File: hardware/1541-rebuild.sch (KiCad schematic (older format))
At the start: 8 parts, among them IC1 ATMEGA1284P-P, P1 1541_CN3, P2 1541_CN4_PIN7_[MOTOR], X1 20Mhz

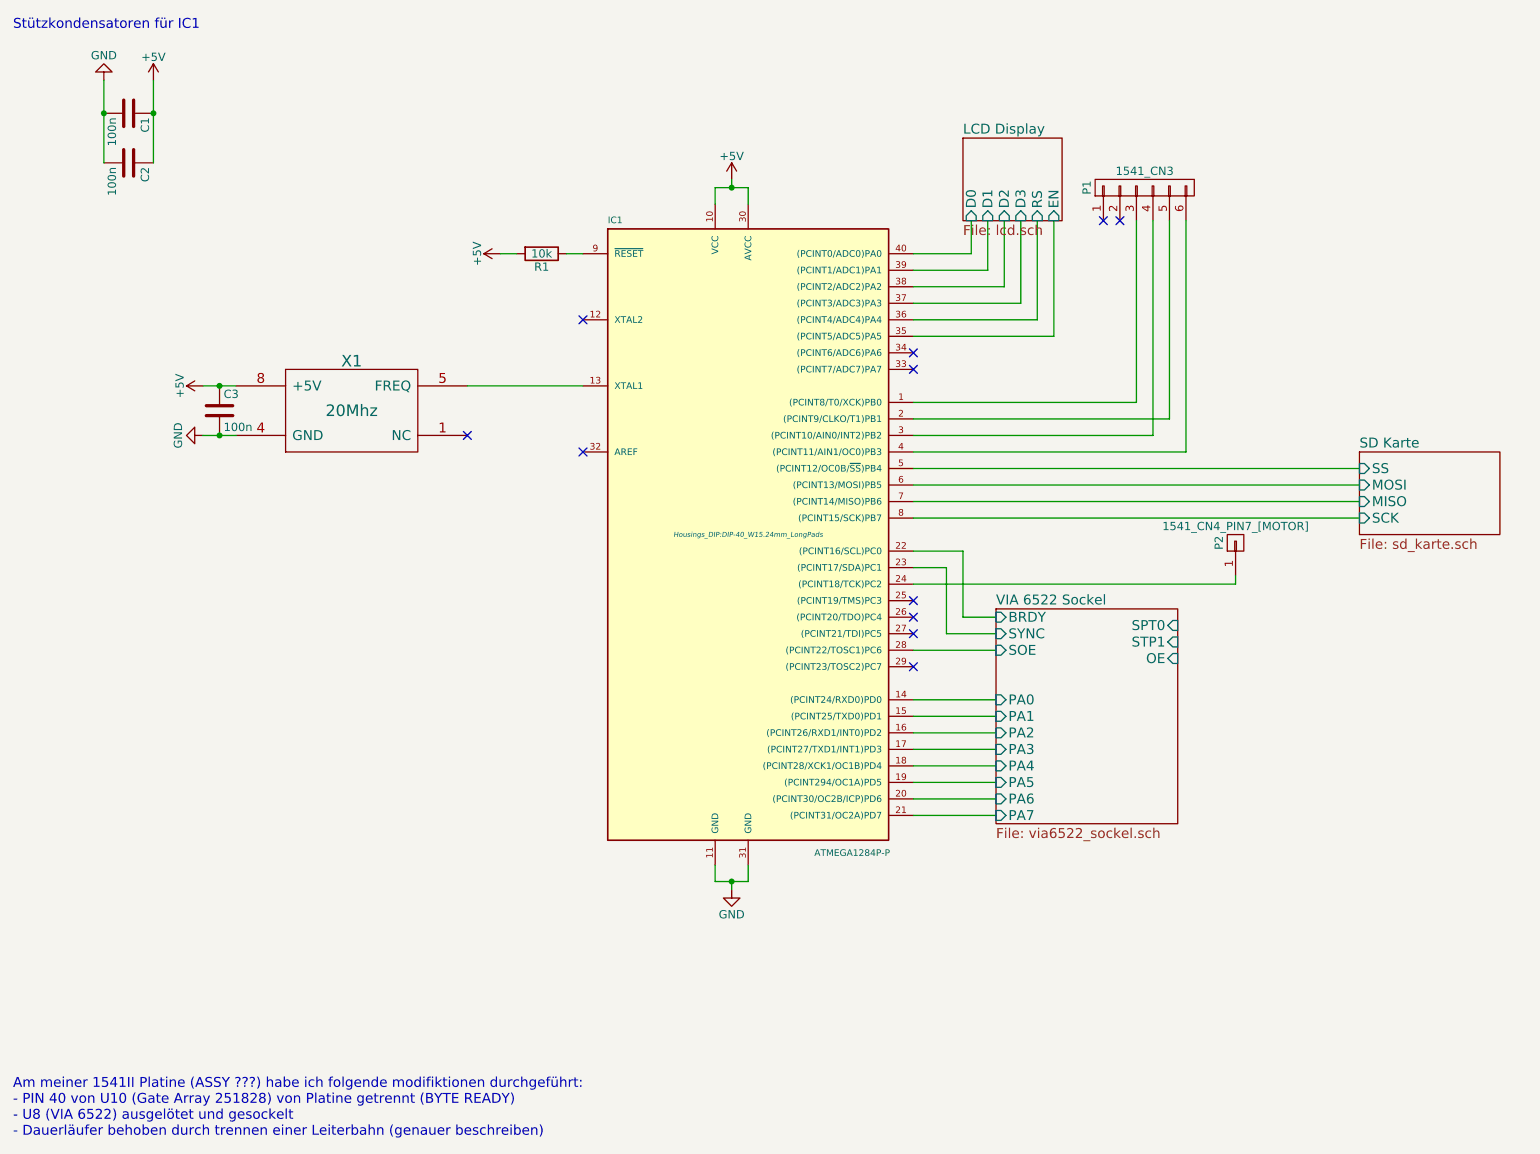
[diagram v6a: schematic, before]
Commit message: Sourcecode neu überarbeitet, Schaltplan angepasst und DOC bearbeitet
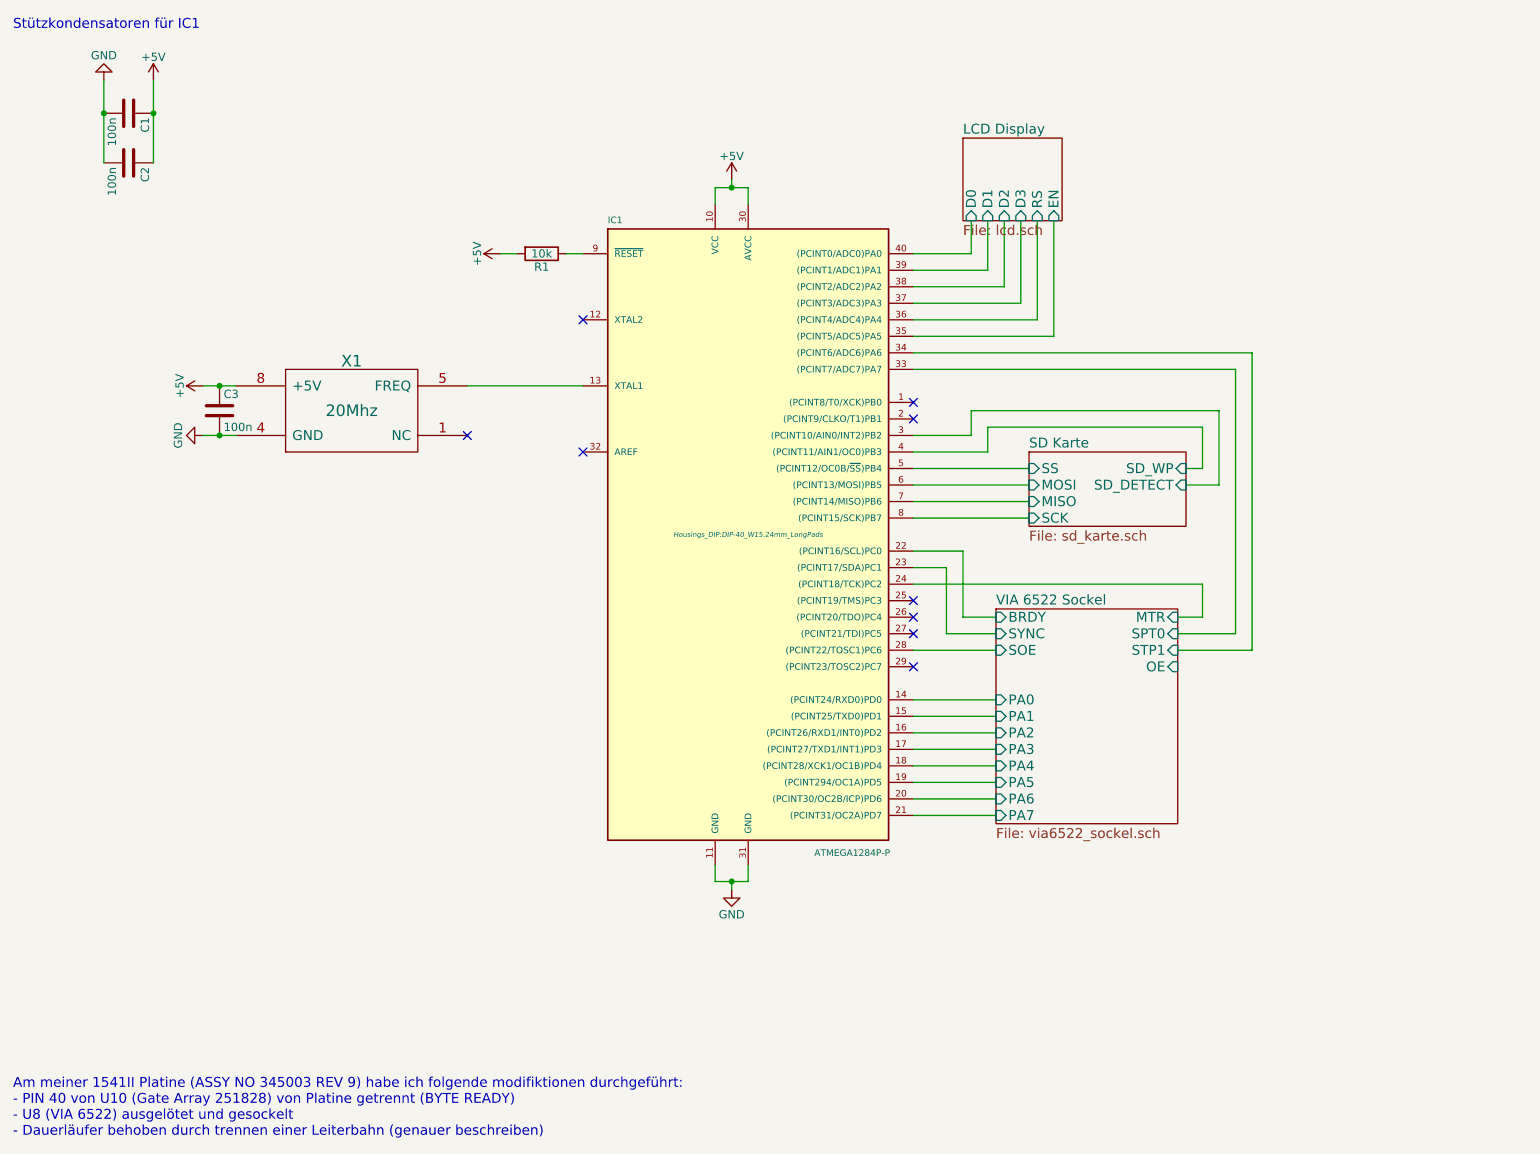
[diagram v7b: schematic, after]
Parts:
- removed P1: 1541_CN3, Socket_Strips:Socket_Strip_Straight_1x06, symbol CONN_01X06
- removed P2: 1541_CN4_PIN7_[MOTOR], Pin_Headers:Pin_Header_Straight_1x01, symbol CONN_01X01
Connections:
- net VIA 6522 Sockel/SPT0: now also IC1.33 ((PCINT7/ADC7)PA7)
- net VIA 6522 Sockel/STP1: now also IC1.34 ((PCINT6/ADC6)PA6)
- net VIA 6522 Sockel/MTR: now reaches IC1.24 ((PCINT18/TCK)PC2)
- net SD Karte/SD_DETECT: now reaches IC1.3 ((PCINT10/AIN0/INT2)PB2)
- net SD Karte/SD_WP: now reaches IC1.4 ((PCINT11/AIN1/OC0)PB3)
- no-connect marks 11 -> 9
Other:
- note added: "Am meiner 1541II Platine (ASSY NO 345003 REV 9) habe ich folgende modifiktionen durchgeführt:\n- PIN 40 von U10 (Gate Array 251828) von Platine getrennt (BYTE READY)\n- U8 (VIA 6522) ausgelötet und gesockelt\n- Dauerläufer behoben durch trennen einer Leiterbahn (genauer beschreiben)"
- note removed: "Am meiner 1541II Platine (ASSY ???) habe ich folgende modifiktionen durchgeführt:\n- PIN 40 von U10 (Gate Array 251828) von Platine getrennt (BYTE READY)\n- U8 (VIA 6522) ausgelötet und gesockelt\n- Dauerläufer behoben durch trennen einer Leiterbahn (genauer beschreiben)"
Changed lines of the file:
@@
 $EndComp
 Text Notes 650  7450 0    60   ~ 0
-Am meiner 1541II Platine (ASSY ???) habe ich folgende modifiktionen durchgeführt:\n- PIN 40 von U10 (Gate Array 251828) von Platine getrennt (BYTE READY)\n- U8 (VIA 6522) ausgelötet und gesockelt\n- Dauerläufer behoben durch trennen einer Leiterbahn (genauer beschreiben)
+Am meiner 1541II Platine (ASSY NO 345003 REV 9) habe ich folgende modifiktionen durchgeführt:\n- PIN 40 von U10 (Gate Array 251828) von Platine getrennt (BYTE READY)\n- U8 (VIA 6522) ausgelötet und gesockelt\n- Dauerläufer behoben durch trennen einer Leiterbahn (genauer beschreiben)
 $Comp
 L TCXO3 X1
@@
 	1    0    0    -1
 $EndComp
-Wire Wire Line
-	3400 2900 4100 2900
 NoConn ~ 3400 3200
 $Comp
@@
 	1    0    0    -1
 $EndComp
-Wire Wire Line
-	1800 2900 2000 2900
-Connection ~ 1900 2900
-Wire Wire Line
-	1800 3200 2000 3200
-Connection ~ 1900 3200
 NoConn ~ 4100 2500
 $Comp
@@
 	1    0    0    -1
 $EndComp
-Wire Wire Line
-	4900 5800 4900 5900
-Wire Wire Line
-	4900 5900 5100 5900
-Wire Wire Line
-	5000 5900 5000 5950
-Wire Wire Line
-	5100 5900 5100 5800
-Connection ~ 5000 5900
 $Comp
 L +5V #PWR04
@@
 	1    0    0    -1
 $EndComp
-Wire Wire Line
-	4900 1800 4900 1700
-Wire Wire Line
-	4900 1700 5100 1700
-Wire Wire Line
-	5000 1700 5000 1650
-Wire Wire Line
-	5100 1700 5100 1800
-Connection ~ 5000 1700
 NoConn ~ 4100 3300
 $Comp
@@
 	0    -1   -1   0
 $EndComp
-Wire Wire Line
-	3700 2100 3600 2100
-Wire Wire Line
-	4000 2100 4100 2100
 $Comp
 L C C1
@@
 	-1   0    0    1
 $EndComp
-Wire Wire Line
-	1200 1050 1200 1550
-Connection ~ 1200 1250
-Wire Wire Line
-	1500 1050 1500 1550
-Connection ~ 1500 1250
 Text Notes 650  750  0    60   ~ 0
 Stützkondensatoren für IC1
-Wire Wire Line
-	6100 3400 8800 3400
-Wire Wire Line
-	6100 3500 8800 3500
-Wire Wire Line
-	6100 3600 8800 3600
-Wire Wire Line
-	6100 3700 8800 3700
 $Sheet
-S 8800 3300 850  500
+S 6800 3300 950  450
 U 55F7A0F9
 F0 "SD Karte" 60
 F1 "sd_karte.sch" 60
-F2 "MISO" I L 8800 3600 60
-F3 "SCK" I L 8800 3700 60
-F4 "MOSI" I L 8800 3500 60
-F5 "SS" I L 8800 3400 60
+F2 "MISO" I L 6800 3600 60
+F3 "SCK" I L 6800 3700 60
+F4 "MOSI" I L 6800 3500 60
+F5 "SS" I L 6800 3400 60
+F6 "SD_DETECT" I R 7750 3500 60
+F7 "SD_WP" I R 7750 3400 60
 $EndSheet
-$Comp
-L CONN_01X06 P1
-U 1 1 55F8E45C
-P 7500 1700
-F 0 "P1" H 7500 2050 50  0000 C CNN
-F 1 "1541_CN3" V 7600 1700 50  0000 C CNN
-F 2 "Socket_Strips:Socket_Strip_Straight_1x06" H 7500 1700 60  0001 C CNN
-F 3 "" H 7500 1700 60  0000 C CNN
-	1    7500 1700
-	0    -1   -1   0
-$EndComp
-Wire Wire Line
-	7450 1900 7450 3000
-Wire Wire Line
-	7450 3000 6100 3000
-Wire Wire Line
-	6100 3100 7650 3100
-Wire Wire Line
-	7650 3100 7650 1900
-Wire Wire Line
-	6100 3200 7550 3200
-Wire Wire Line
-	7550 3200 7550 1900
-Wire Wire Line
-	6100 3300 7750 3300
-Wire Wire Line
-	7750 3300 7750 1900
 $Sheet
 S 6400 1400 600  500
@@
 F7 "EN" I B 6950 1900 60
 $EndSheet
-Wire Wire Line
-	6450 1900 6450 2100
-Wire Wire Line
-	6450 2100 6100 2100
-Wire Wire Line
-	6550 1900 6550 2200
-Wire Wire Line
-	6550 2200 6100 2200
-Wire Wire Line
-	6650 1900 6650 2300
-Wire Wire Line
-	6650 2300 6100 2300
-Wire Wire Line
-	6750 1900 6750 2400
-Wire Wire Line
-	6750 2400 6100 2400
-Wire Wire Line
-	6850 1900 6850 2500
-Wire Wire Line
-	6850 2500 6100 2500
-Wire Wire Line
-	6950 1900 6950 2600
-Wire Wire Line
-	6950 2600 6100 2600
-NoConn ~ 7250 1900
-NoConn ~ 7350 1900
-NoConn ~ 6100 2700
-NoConn ~ 6100 2800
 NoConn ~ 6100 4200
 NoConn ~ 6100 4300
@@
 F9 "PA7" I L 6600 5500 60
 F10 "BRDY" I L 6600 4300 60
-F11 "SPT0" I R 7700 4350 60
-F12 "STP1" I R 7700 4450 60
+F11 "SPT0" I R 7700 4400 60
+F12 "STP1" I R 7700 4500 60
 F13 "SYNC" I L 6600 4400 60
-F14 "OE" I R 7700 4550 60
+F14 "OE" I R 7700 4600 60
 F15 "SOE" I L 6600 4500 60
+F16 "MTR" I R 7700 4300 60
 $EndSheet
 Wire Wire Line
+	3400 2900 4100 2900
+Wire Wire Line
+	1800 2900 2000 2900
+Connection ~ 1900 2900
+Wire Wire Line
+	1800 3200 2000 3200
+Connection ~ 1900 3200
+Wire Wire Line
+	4900 5800 4900 5900
+Wire Wire Line
+	4900 5900 5100 5900
+Wire Wire Line
+	5000 5900 5000 5950
+Wire Wire Line
+	5100 5900 5100 5800
+Connection ~ 5000 5900
+Wire Wire Line
+	4900 1800 4900 1700
+Wire Wire Line
+	4900 1700 5100 1700
+Wire Wire Line
+	5000 1700 5000 1650
+Wire Wire Line
+	5100 1700 5100 1800
+Connection ~ 5000 1700
+Wire Wire Line
+	3700 2100 3600 2100
+Wire Wire Line
+	4000 2100 4100 2100
+Wire Wire Line
+	1200 1050 1200 1550
+Connection ~ 1200 1250
+Wire Wire Line
+	1500 1050 1500 1550
+Connection ~ 1500 1250
+Wire Wire Line
+	6450 1900 6450 2100
+Wire Wire Line
+	6450 2100 6100 2100
+Wire Wire Line
+	6550 1900 6550 2200
+Wire Wire Line
+	6550 2200 6100 2200
+Wire Wire Line
+	6650 1900 6650 2300
+Wire Wire Line
+	6650 2300 6100 2300
+Wire Wire Line
+	6750 1900 6750 2400
+Wire Wire Line
+	6750 2400 6100 2400
+Wire Wire Line
+	6850 1900 6850 2500
+Wire Wire Line
+	6850 2500 6100 2500
+Wire Wire Line
+	6950 1900 6950 2600
+Wire Wire Line
+	6950 2600 6100 2600
+Wire Wire Line
 	6100 4800 6600 4800
 Wire Wire Line
@@
 Wire Wire Line
 	6400 4300 6600 4300
-$Comp
-L CONN_01X01 P2
-U 1 1 55F9A2C7
-P 8050 3850
-F 0 "P2" H 8050 3950 50  0000 C CNN
-F 1 "1541_CN4_PIN7_[MOTOR]" V 8150 3850 50  0000 C CNN
-F 2 "Pin_Headers:Pin_Header_Straight_1x01" H 8050 3850 60  0001 C CNN
-F 3 "" H 8050 3850 60  0000 C CNN
-	1    8050 3850
-	0    -1   -1   0
-$EndComp
-Wire Wire Line
-	6100 4100 8050 4100
-Wire Wire Line
-	8050 4100 8050 4050
+Wire Wire Line
+	6100 4100 7850 4100
+Wire Wire Line
+	6100 2700 8150 2700
+Wire Wire Line
+	6100 2800 8050 2800
+Wire Wire Line
+	8150 2700 8150 4500
+Wire Wire Line
+	8050 2800 8050 4400
+Wire Wire Line
+	8050 4400 7700 4400
+Wire Wire Line
+	8150 4500 7700 4500
+Wire Wire Line
+	7850 4100 7850 4300
+Wire Wire Line
+	7850 4300 7700 4300
+Wire Wire Line
+	6100 3400 6800 3400
+Wire Wire Line
+	6100 3500 6800 3500
+Wire Wire Line
+	6100 3600 6800 3600
+Wire Wire Line
+	6100 3700 6800 3700
+Wire Wire Line
+	6100 3300 6550 3300
+Wire Wire Line
+	6550 3300 6550 3150
+Wire Wire Line
+	6550 3150 7850 3150
+Wire Wire Line
+	7850 3150 7850 3400
+Wire Wire Line
+	7850 3400 7750 3400
+Wire Wire Line
+	6100 3200 6450 3200
+Wire Wire Line
+	6450 3200 6450 3050
+Wire Wire Line
+	6450 3050 7950 3050
+Wire Wire Line
+	7950 3050 7950 3500
+Wire Wire Line
+	7950 3500 7750 3500
+NoConn ~ 6100 3000
+NoConn ~ 6100 3100
 $EndSCHEMATC

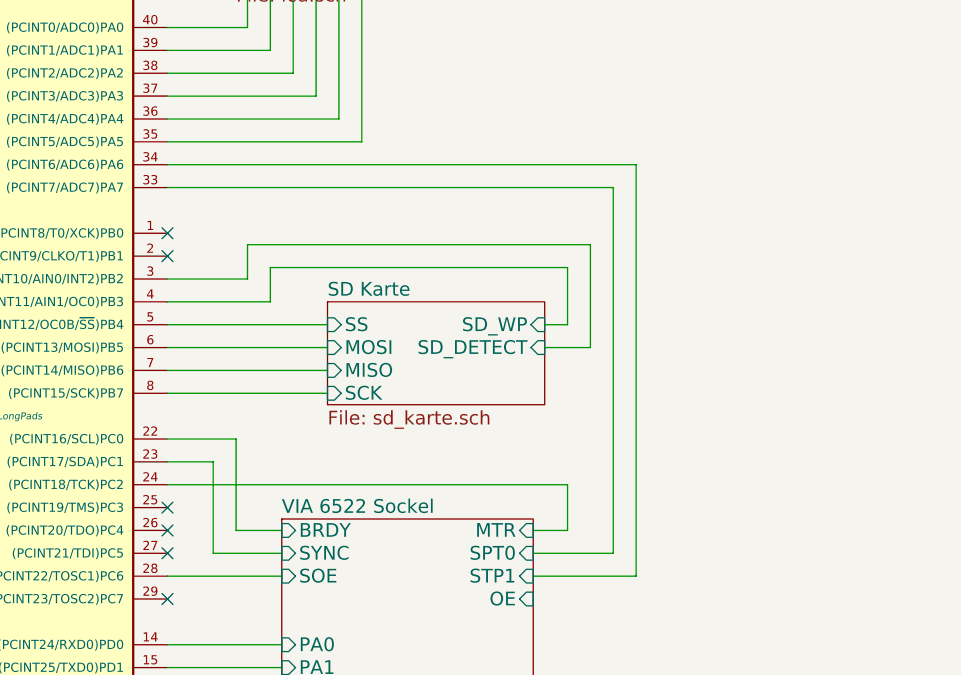
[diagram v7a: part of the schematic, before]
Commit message: Schaltplan angepasst und Firmware angepasst
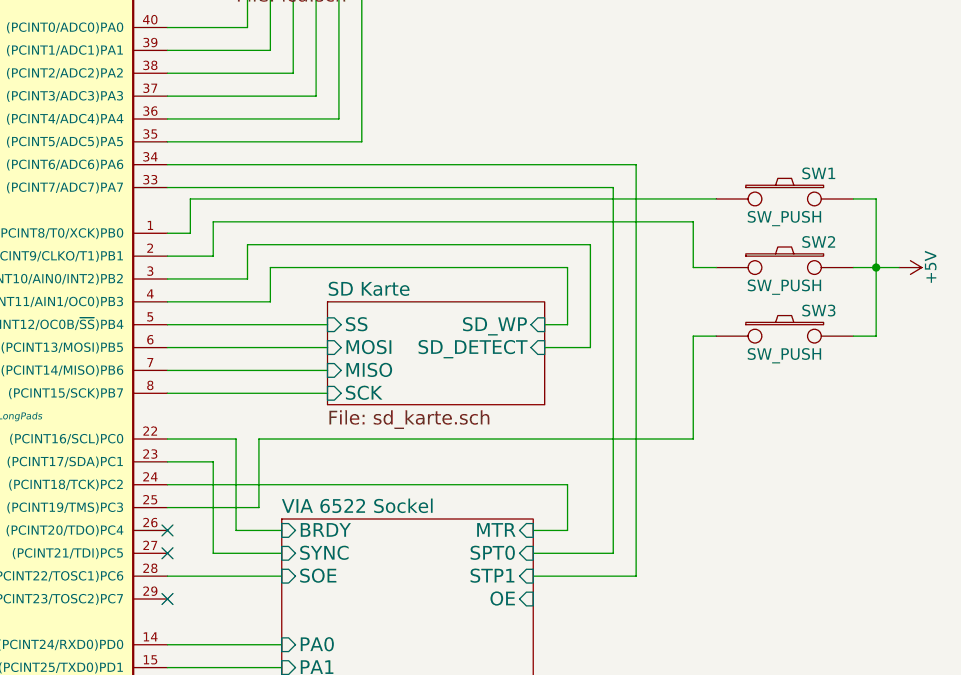
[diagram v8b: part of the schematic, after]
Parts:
- added SW1, SW2, SW3: SW_PUSH, symbol SW_PUSH
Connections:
- net +5V: now also SW1.2, SW2.2, SW3.2
- net at IC1.1 ((PCINT8/T0/XCK)PB0): now also SW1.1
- net at IC1.2 ((PCINT9/CLKO/T1)PB1): now also SW2.1
- net at IC1.25 ((PCINT19/TMS)PC3): now also SW3.1
- no-connect marks 9 -> 6
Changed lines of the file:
@@
 F7 "EN" I B 6950 1900 60
 $EndSheet
-NoConn ~ 6100 4200
 NoConn ~ 6100 4300
 NoConn ~ 6100 4400
@@
 Wire Wire Line
 	7950 3500 7750 3500
-NoConn ~ 6100 3000
-NoConn ~ 6100 3100
+$Comp
+L SW_PUSH SW1
+U 1 1 55FEAE1B
+P 8800 2850
+F 0 "SW1" H 8950 2960 50  0000 C CNN
+F 1 "SW_PUSH" H 8800 2770 50  0000 C CNN
+F 2 "" H 8800 2850 60  0000 C CNN
+F 3 "" H 8800 2850 60  0000 C CNN
+	1    8800 2850
+	1    0    0    -1
+$EndComp
+$Comp
+L SW_PUSH SW2
+U 1 1 55FEAF42
+P 8800 3150
+F 0 "SW2" H 8950 3260 50  0000 C CNN
+F 1 "SW_PUSH" H 8800 3070 50  0000 C CNN
+F 2 "" H 8800 3150 60  0000 C CNN
+F 3 "" H 8800 3150 60  0000 C CNN
+	1    8800 3150
+	1    0    0    -1
+$EndComp
+$Comp
+L +5V #PWR08
+U 1 1 55FEB137
+P 9300 3150
+F 0 "#PWR08" H 9300 3000 50  0001 C CNN
+F 1 "+5V" H 9300 3290 50  0000 C CNN
+F 2 "" H 9300 3150 60  0000 C CNN
+F 3 "" H 9300 3150 60  0000 C CNN
+	1    9300 3150
+	0    1    1    0
+$EndComp
+Wire Wire Line
+	9100 2850 9200 2850
+Wire Wire Line
+	9200 2850 9200 3450
+Wire Wire Line
+	9100 3150 9300 3150
+Connection ~ 9200 3150
+Wire Wire Line
+	6100 3000 6200 3000
+Wire Wire Line
+	6200 3000 6200 2850
+Wire Wire Line
+	6200 2850 8500 2850
+Wire Wire Line
+	6100 3100 6300 3100
+Wire Wire Line
+	6300 3100 6300 2950
+Wire Wire Line
+	6300 2950 8400 2950
+Wire Wire Line
+	8400 2950 8400 3150
+Wire Wire Line
+	8400 3150 8500 3150
+$Comp
+L SW_PUSH SW3
+U 1 1 55FECA06
+P 8800 3450
+F 0 "SW3" H 8950 3560 50  0000 C CNN
+F 1 "SW_PUSH" H 8800 3370 50  0000 C CNN
+F 2 "" H 8800 3450 60  0000 C CNN
+F 3 "" H 8800 3450 60  0000 C CNN
+	1    8800 3450
+	1    0    0    -1
+$EndComp
+Wire Wire Line
+	9200 3450 9100 3450
+Wire Wire Line
+	6100 4200 6500 4200
+Wire Wire Line
+	6500 4200 6500 3900
+Wire Wire Line
+	6500 3900 8400 3900
+Wire Wire Line
+	8400 3900 8400 3450
+Wire Wire Line
+	8400 3450 8500 3450
 $EndSCHEMATC
